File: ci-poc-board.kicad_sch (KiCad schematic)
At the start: 14 parts, among them SW1 SW_Push

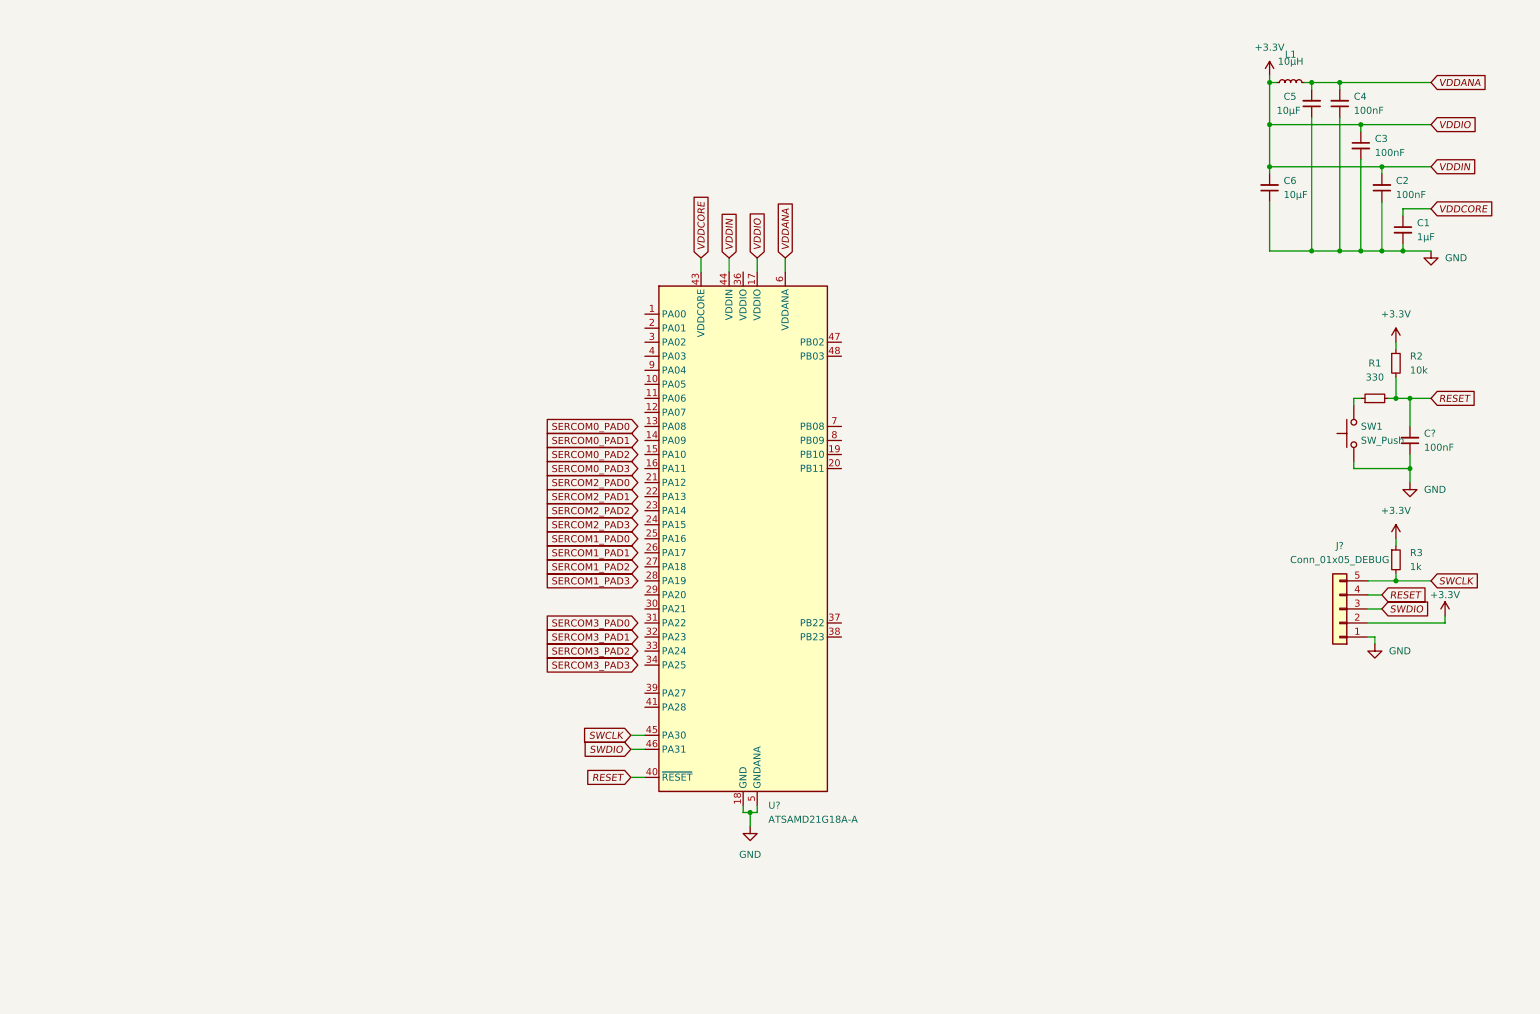
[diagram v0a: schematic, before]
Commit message: USART, SPI en I2C connecties gemaakt. OSC toegevoegd. JTAG ICE compatible interface toegevoegd.
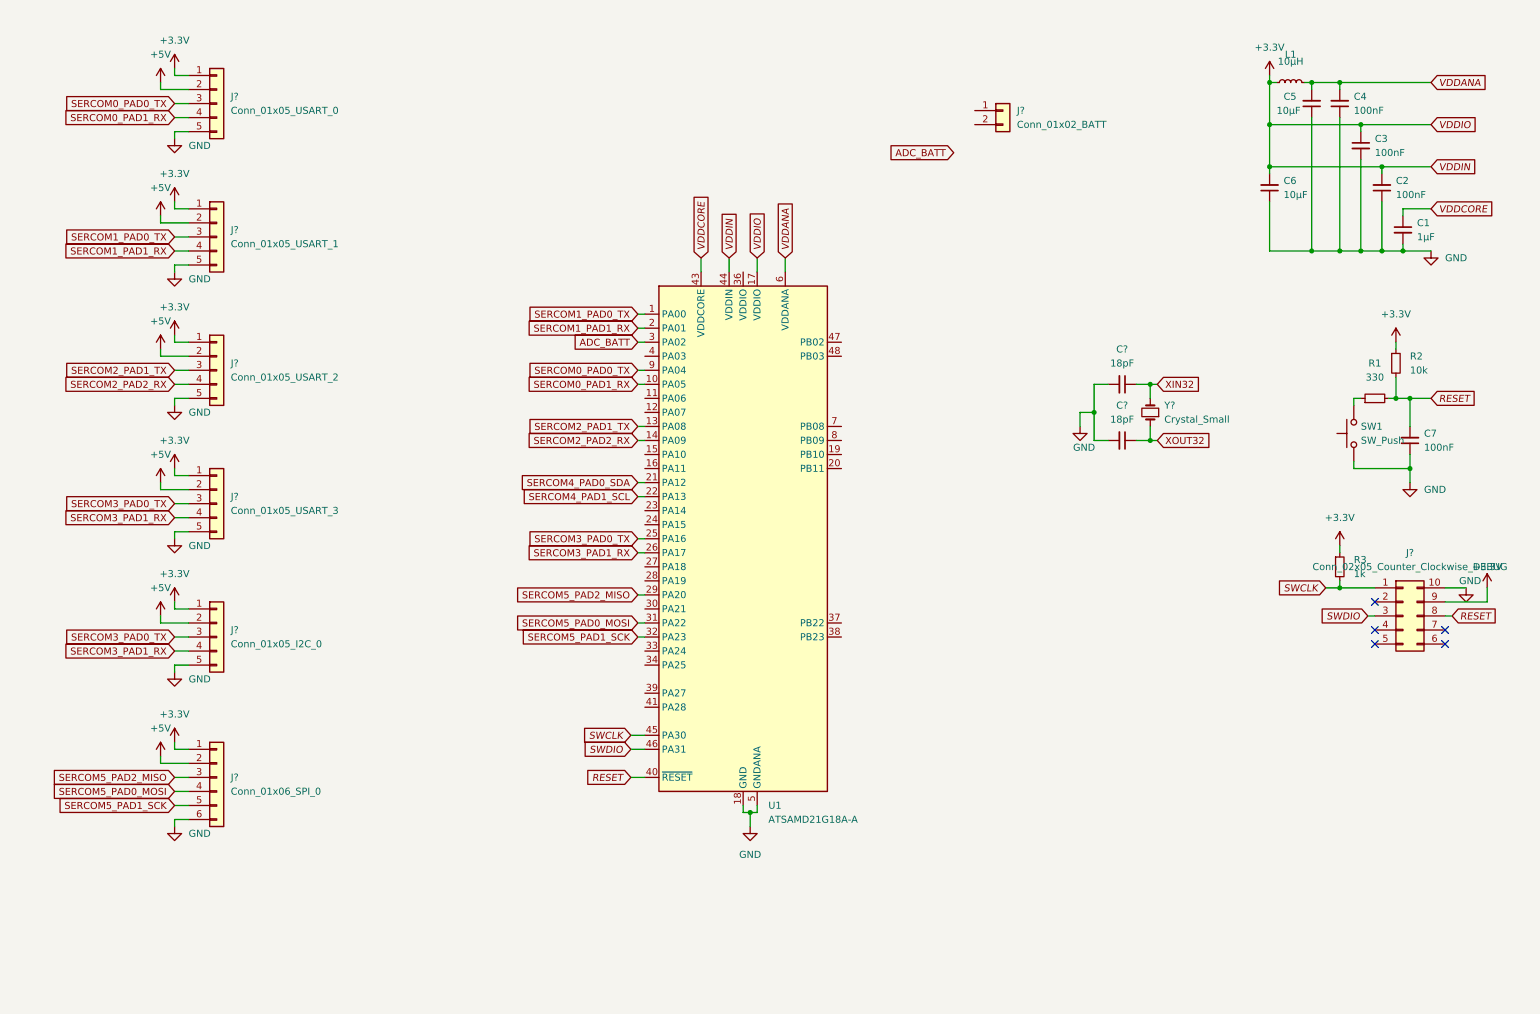
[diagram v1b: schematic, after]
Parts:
- removed J?: Conn_01x05_DEBUG, symbol Connector_Generic:Conn_01x05
- added C? (x2): 18pF, symbol Device:C_Small
- added J?: Conn_02x05_Counter_Clockwise_DEBUG, symbol Connector_Generic:Conn_02x05_Counter_Clockwise
- added J?: Conn_01x05_USART_0, symbol Connector_Generic:Conn_01x05
- added J?: Conn_01x05_USART_3, symbol Connector_Generic:Conn_01x05
- added J?: Conn_01x05_USART_2, symbol Connector_Generic:Conn_01x05
- added J?: Conn_01x05_USART_1, symbol Connector_Generic:Conn_01x05
- added J?: Conn_01x02_BATT, Connector_JST:JST_PH_B2B-PH-K_1x02_P2.00mm_Vertical, symbol Connector_Generic:Conn_01x02
- added J?: Conn_01x06_SPI_0, symbol Connector_Generic:Conn_01x06
- added J?: Conn_01x05_I2C_0, symbol Connector_Generic:Conn_01x05
- added Y?: Crystal_Small, symbol Device:Crystal_Small
- gave numbers to parts that had none: 2
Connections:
- net +3V3: now also J?.1 (Pin_1), J?.1 (Pin_1), J?.1 (Pin_1), J?.1 (Pin_1), J?.1 (Pin_1), J?.1 (Pin_1), J?.9 (Pin_9)
- net GND: now also C?.2, C?.2, J?.10 (Pin_10), J?.5 (Pin_5), J?.5 (Pin_5), J?.5 (Pin_5), J?.5 (Pin_5), J?.5 (Pin_5), J?.6 (Pin_6)
- net RESET: now also J?.8 (Pin_8)
- net SWCLK: now also J?.1 (Pin_1)
- net SWDIO: now also J?.3 (Pin_3)
- net SERCOM1_PAD0_TX: now reaches U1.1 (PA00)
- net SERCOM1_PAD0_TX: now also J?.3 (Pin_3)
- net SERCOM0_PAD1_RX: now reaches U1.10 (PA05)
- net SERCOM0_PAD1_RX: now also J?.4 (Pin_4)
- net SERCOM2_PAD1_TX: now reaches U1.13 (PA08)
- net SERCOM2_PAD1_TX: now also J?.3 (Pin_3)
- net SERCOM2_PAD2_RX: now reaches U1.14 (PA09)
- net SERCOM2_PAD2_RX: now also J?.4 (Pin_4)
- net SERCOM1_PAD1_RX: now reaches U1.2 (PA01)
- net SERCOM1_PAD1_RX: now also J?.4 (Pin_4)
- net SERCOM4_PAD0_SDA: now reaches U1.21 (PA12)
- net SERCOM4_PAD1_SCL: now reaches U1.22 (PA13)
- net SERCOM3_PAD0_TX: now reaches U1.25 (PA16)
- net SERCOM3_PAD0_TX: now also J?.3 (Pin_3), J?.3 (Pin_3)
- net SERCOM3_PAD1_RX: now reaches U1.26 (PA17)
- net SERCOM3_PAD1_RX: now also J?.4 (Pin_4), J?.4 (Pin_4)
- net SERCOM5_PAD2_MISO: now reaches U1.29 (PA20)
- net SERCOM5_PAD2_MISO: now also J?.3 (Pin_3)
- net ADC_BATT: now reaches U1.3 (PA02)
- net SERCOM5_PAD0_MOSI: now reaches U1.31 (PA22)
- net SERCOM5_PAD0_MOSI: now also J?.4 (Pin_4)
- net SERCOM5_PAD1_SCK: now reaches U1.32 (PA23)
- net SERCOM5_PAD1_SCK: now also J?.5 (Pin_5)
- net SERCOM0_PAD0_TX: now reaches U1.9 (PA04)
- net SERCOM0_PAD0_TX: now also J?.3 (Pin_3)
- new net +5V: J?.2 (Pin_2), J?.2 (Pin_2), J?.2 (Pin_2), J?.2 (Pin_2), J?.2 (Pin_2), J?.2 (Pin_2)
- new net XIN32: C?.1, Y?.2
- new net XOUT32: C?.1, Y?.1
- no-connect marks 0 -> 5
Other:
- moved on the sheet: R3

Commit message: Added RN2483 LoRa Module, battery connection, oscillator, 3.3V and 5V regulator. Removed SPI
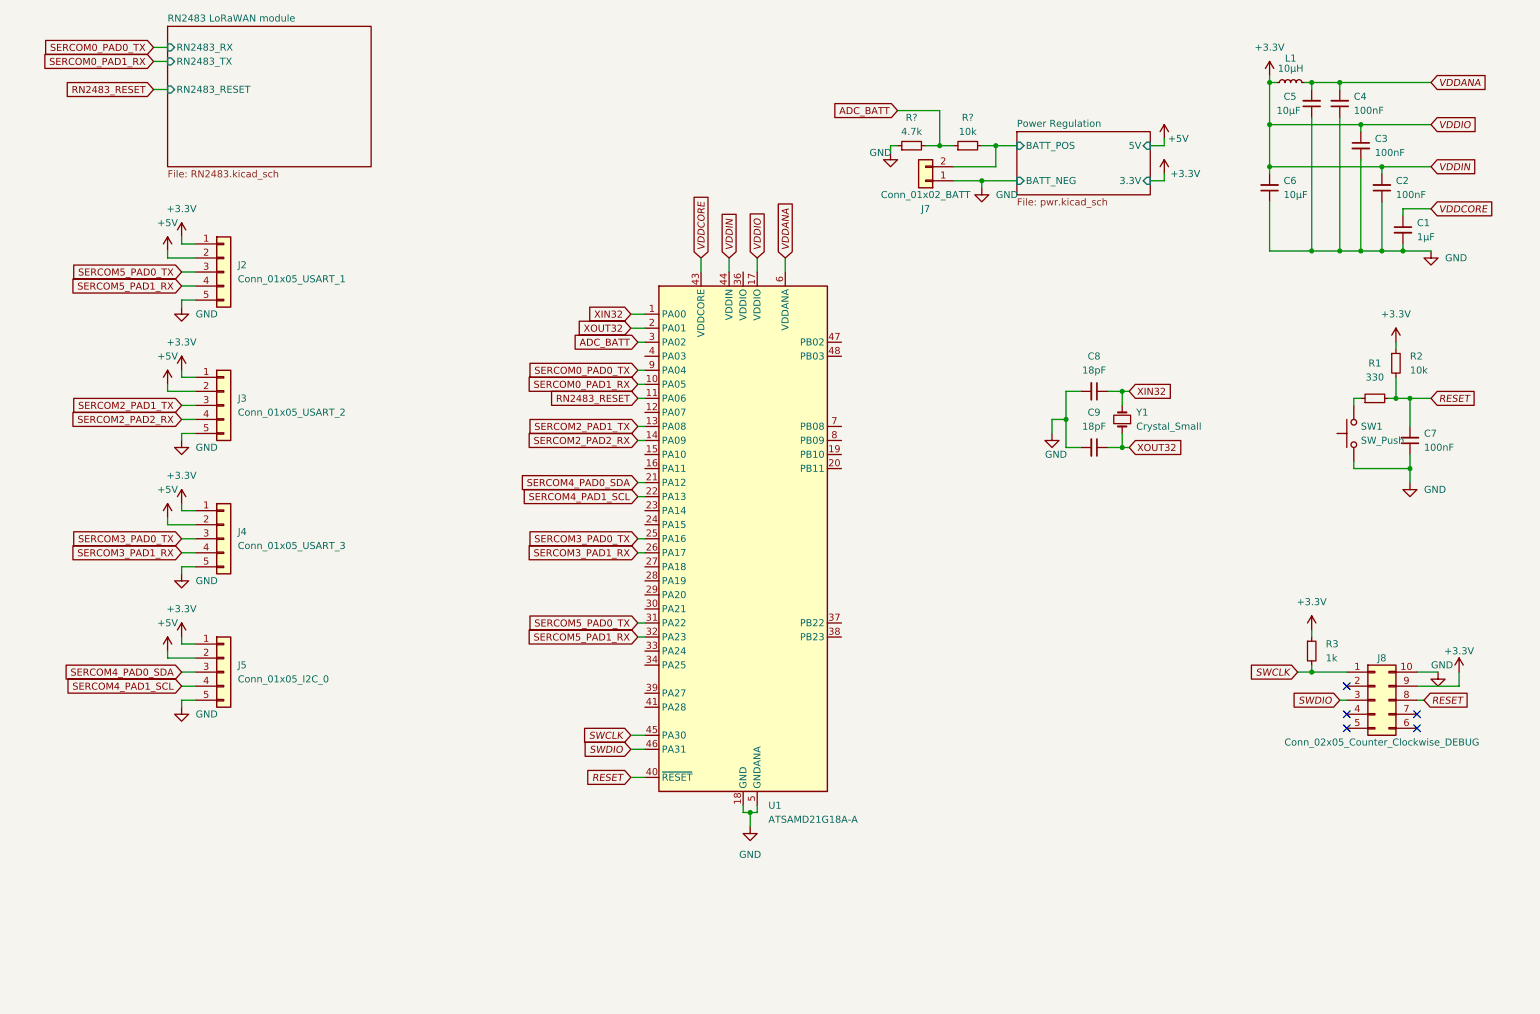
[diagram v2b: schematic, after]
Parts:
- removed J?: Conn_01x05_USART_0, symbol Connector_Generic:Conn_01x05
- removed J?: Conn_01x06_SPI_0, symbol Connector_Generic:Conn_01x06
- added R?: 4.7k, symbol Device:R_Small
- added R?: 10k, symbol Device:R_Small
- gave numbers to parts that had none: 9
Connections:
- net SERCOM5_PAD0_MOSI is gone; now on net SERCOM5_PAD0_TX: U1.31 (PA22)
- net SERCOM5_PAD1_SCK is gone; now on net SERCOM5_PAD1_RX: U1.32 (PA23)
- net ADC_BATT: now also R?.1, R?.2
- net GND: now also J7.1 (Pin_1), R?.1
- net SERCOM3_PAD0_TX: no longer J5.3 (Pin_3)
- net SERCOM3_PAD1_RX: no longer J5.4 (Pin_4)
- net SERCOM4_PAD0_SDA: now also J5.3 (Pin_3)
- net SERCOM4_PAD1_SCL: now also J5.4 (Pin_4)
- net XIN32: now also U1.1 (PA00)
- net XOUT32: now also U1.2 (PA01)
- net RN2483_RESET: now reaches U1.11 (PA06)
- net Power Regulation/BATT_POS: now reaches J7.2 (Pin_2)
- net Power Regulation/BATT_POS: now also R?.2
- net SERCOM1_PAD0_TX renamed SERCOM5_PAD0_TX
- net SERCOM5_PAD0_TX: no longer U1.1 (PA00)
- net SERCOM1_PAD1_RX renamed SERCOM5_PAD1_RX
- net SERCOM5_PAD1_RX: no longer U1.2 (PA01)
- net SERCOM5_PAD2_MISO: no longer names the net of U1.29 (PA20)
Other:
- added sheet Power Regulation (pwr.kicad_sch)
- added sheet RN2483 LoRaWAN module (RN2483.kicad_sch)
- moved on the sheet: C8, C9, J2, J3, J4, J5, J7, J8, R3, Y1

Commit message: Finishing schematic, first iteration of PCB
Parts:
- added H1, H2, H3, H4: MountingHole_Pad, MountingHole:MountingHole_2.1mm, symbol Mechanical:MountingHole_Pad
- added R6, R7: ?, Resistor_SMD:R_0805_2012Metric_Pad1.20x1.40mm_HandSolder, symbol Device:R_Small
- C1, C2, C3, C4, C5, C6, C7, C8, C9: footprint (none) -> Capacitor_SMD:C_0805_2012Metric_Pad1.18x1.45mm_HandSolder
- J2, J3, J4, J5: footprint (none) -> Connector_JST:JST_XH_B5B-XH-A_1x05_P2.50mm_Vertical
- J8: footprint (none) -> Connector_PinHeader_2.54mm:PinHeader_2x05_P2.54mm_Vertical
- L1: footprint (none) -> Inductor_SMD:L_Murata_LQH2MCNxxxx02_2.0x1.6mm
- R1, R2, R3: footprint (none) -> Resistor_SMD:R_0805_2012Metric_Pad1.20x1.40mm_HandSolder
- R4, R5: renamed from R?; footprint (none) -> Resistor_SMD:R_0805_2012Metric_Pad1.20x1.40mm_HandSolder
- SW1: footprint (none) -> Button_Switch_SMD:SW_Push_1P1T_NO_6x6mm_H9.5mm
- Y1: footprint (none) -> Crystal:Crystal_SMD_3215-2Pin_3.2x1.5mm
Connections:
- net +3V3: now also R6.1, R7.1
- net GND: now also H1.1, H2.1, H3.1, H4.1
- net SERCOM4_PAD0_SDA: now also R6.2
- net SERCOM4_PAD1_SCL: now also R7.2
- no-connect marks 5 -> 28

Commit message: Small changes. Added BOM
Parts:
- H1, H2, H3, H4: footprint MountingHole:MountingHole_2.1mm -> MountingHole:MountingHole_3.2mm_M3_DIN965_Pad
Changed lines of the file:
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@@
     (property "Reference" "H4" (id 0) (at 21.59 189.23 90))
     (property "Value" "MountingHole_Pad" (id 1) (at 29.21 191.77 90))
-    (property "Footprint" "MountingHole:MountingHole_2.1mm" (id 2) (at 20.32 190.5 0)
+    (property "Footprint" "MountingHole:MountingHole_3.2mm_M3_DIN965_Pad" (id 2) (at 20.32 190.5 0)
       (effects (font (size 1.27 1.27)) hide)
     )
@@
     (property "Reference" "H3" (id 0) (at 21.59 184.15 90))
     (property "Value" "MountingHole_Pad" (id 1) (at 29.21 186.69 90))
-    (property "Footprint" "MountingHole:MountingHole_2.1mm" (id 2) (at 20.32 185.42 0)
+    (property "Footprint" "MountingHole:MountingHole_3.2mm_M3_DIN965_Pad" (id 2) (at 20.32 185.42 0)
       (effects (font (size 1.27 1.27)) hide)
     )
@@
     (property "Reference" "H2" (id 0) (at 21.59 179.07 90))
     (property "Value" "MountingHole_Pad" (id 1) (at 29.21 181.61 90))
-    (property "Footprint" "MountingHole:MountingHole_2.1mm" (id 2) (at 20.32 180.34 0)
+    (property "Footprint" "MountingHole:MountingHole_3.2mm_M3_DIN965_Pad" (id 2) (at 20.32 180.34 0)
       (effects (font (size 1.27 1.27)) hide)
     )
@@
     (property "Reference" "H1" (id 0) (at 21.59 173.99 90))
     (property "Value" "MountingHole_Pad" (id 1) (at 29.21 176.53 90))
-    (property "Footprint" "MountingHole:MountingHole_2.1mm" (id 2) (at 20.32 175.26 0)
+    (property "Footprint" "MountingHole:MountingHole_3.2mm_M3_DIN965_Pad" (id 2) (at 20.32 175.26 0)
       (effects (font (size 1.27 1.27)) hide)
     )
@@
     )
     (path "/b8c78488-74d4-4889-8e22-2e83f9b484cb"
-      (reference "H1") (unit 1) (value "MountingHole_Pad") (footprint "MountingHole:MountingHole_2.1mm")
+      (reference "H1") (unit 1) (value "MountingHole_Pad") (footprint "MountingHole:MountingHole_3.2mm_M3_DIN965_Pad")
     )
     (path "/64dd8659-9f45-48e0-88e6-48f6f36c0757"
-      (reference "H2") (unit 1) (value "MountingHole_Pad") (footprint "MountingHole:MountingHole_2.1mm")
+      (reference "H2") (unit 1) (value "MountingHole_Pad") (footprint "MountingHole:MountingHole_3.2mm_M3_DIN965_Pad")
     )
     (path "/34d66f95-94ed-4979-83df-962a806e9a20"
-      (reference "H3") (unit 1) (value "MountingHole_Pad") (footprint "MountingHole:MountingHole_2.1mm")
+      (reference "H3") (unit 1) (value "MountingHole_Pad") (footprint "MountingHole:MountingHole_3.2mm_M3_DIN965_Pad")
     )
     (path "/206d36e0-8612-4c8c-bb5b-c8af7708345e"
-      (reference "H4") (unit 1) (value "MountingHole_Pad") (footprint "MountingHole:MountingHole_2.1mm")
+      (reference "H4") (unit 1) (value "MountingHole_Pad") (footprint "MountingHole:MountingHole_3.2mm_M3_DIN965_Pad")
     )
     (path "/0c5c10ee-9703-4200-bd24-bfb398e648cb/2a9b7790-e061-4cb7-8be5-f0cfa965097e"
@@
     )
     (path "/0c5c10ee-9703-4200-bd24-bfb398e648cb/28d92d15-cab4-47a1-a503-7ca41978f72a"
-      (reference "MODULE1") (unit 1) (value "RN2483-I_RM095-RN2483-I_RM095") (footprint "RN2483:RN2483A-I&slash_RM105")
+      (reference "MODULE1") (unit 1) (value "RN2483-I_RM095-RN2483-I_RM095") (footprint "RF_Module:RN2483")
     )
     (path "/cd514f6c-36ad-4771-b7ab-00b3522935d0"

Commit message: Edited documentation
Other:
- title: (none) -> Main Schematic
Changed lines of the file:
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@@
 (kicad_sch (version 20211123) (generator eeschema)
   (paper "A4")
+  (title_block
+    (title "Main Schematic")
+    (date "2022-03-10")
+    (rev "1.0")
+  )
   (junction (at 237.49 35.56) (diameter 0) (color 0 0 0 0)
   )
